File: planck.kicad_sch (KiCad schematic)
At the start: 53 parts, among them J1 USB_C_Receptacle_USB2.0, K1 KEYSW, K2 KEYSW, K3 KEYSW, K4 KEYSW, SW1 SW_PUSH, U1 ATmega32U4-M, Y1 Crystal_GND24_Small

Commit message: finishing it off
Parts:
- removed TP10: PB5, TestPoint:TestPoint_Pad_D1.0mm, symbol Connector:TestPoint
- removed TP11: PB6, TestPoint:TestPoint_Pad_D1.0mm, symbol Connector:TestPoint
- removed TP12: PB7, TestPoint:TestPoint_Pad_D1.0mm, symbol Connector:TestPoint
- removed TP13: PC6, TestPoint:TestPoint_Pad_D1.0mm, symbol Connector:TestPoint
- removed TP14: PC7, TestPoint:TestPoint_Pad_D1.0mm, symbol Connector:TestPoint
- removed TP15: PD0, TestPoint:TestPoint_Pad_D1.0mm, symbol Connector:TestPoint
- removed TP16: PD1, TestPoint:TestPoint_Pad_D1.0mm, symbol Connector:TestPoint
- removed TP17: PD2, TestPoint:TestPoint_Pad_D1.0mm, symbol Connector:TestPoint
- removed TP18: PD3, TestPoint:TestPoint_Pad_D1.0mm, symbol Connector:TestPoint
- removed TP19: PD4, TestPoint:TestPoint_Pad_D1.0mm, symbol Connector:TestPoint
- removed TP20: PD6, TestPoint:TestPoint_Pad_D1.0mm, symbol Connector:TestPoint
- removed TP21: PD7, TestPoint:TestPoint_Pad_D1.0mm, symbol Connector:TestPoint
- removed TP22: PE6, TestPoint:TestPoint_Pad_D1.0mm, symbol Connector:TestPoint
- removed TP23: PF6, TestPoint:TestPoint_Pad_D1.0mm, symbol Connector:TestPoint
- removed TP24: PF7, TestPoint:TestPoint_Pad_D1.0mm, symbol Connector:TestPoint
- removed TP4: PD5, TestPoint:TestPoint_Pad_D1.0mm, symbol Connector:TestPoint
- removed TP5: PB0, TestPoint:TestPoint_Pad_D1.0mm, symbol Connector:TestPoint
- removed TP6: PB1, TestPoint:TestPoint_Pad_D1.0mm, symbol Connector:TestPoint
- removed TP7: PB2, TestPoint:TestPoint_Pad_D1.0mm, symbol Connector:TestPoint
- removed TP8: PB3, TestPoint:TestPoint_Pad_D1.0mm, symbol Connector:TestPoint
- removed TP9: PB4, TestPoint:TestPoint_Pad_D1.0mm, symbol Connector:TestPoint
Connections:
- net PB0: no longer names the net of U1.8 (PB0)
- net PB1: no longer names the net of U1.9 (PB1)
- net PB2: no longer names the net of U1.10 (PB2)
- net PB3: no longer names the net of U1.11 (PB3)
- net PB4: no longer names the net of U1.28 (PB4)
- net PB5: no longer names the net of U1.29 (PB5)
- net PB6: no longer names the net of U1.30 (PB6)
- net PB7: no longer names the net of U1.12 (PB7)
- net PC6: no longer names the net of U1.31 (PC6)
- net PC7: no longer names the net of U1.32 (PC7)
- net PD0: no longer names the net of U1.18 (PD0)
- net PD1: no longer names the net of U1.19 (PD1)
- net PD2: no longer names the net of U1.20 (PD2)
- net PD3: no longer names the net of U1.21 (PD3)
- net PD4: no longer names the net of U1.25 (PD4)
- net PD5: no longer names the net of U1.22 (PD5)
- net PD6: no longer names the net of U1.26 (PD6)
- net PD7: no longer names the net of U1.27 (PD7)
- net PE6: no longer names the net of U1.1 (PE6)
- net PF6: no longer names the net of U1.37 (PF6)
- net PF7: no longer names the net of U1.36 (PF7)
- no-connect marks 0 -> 21

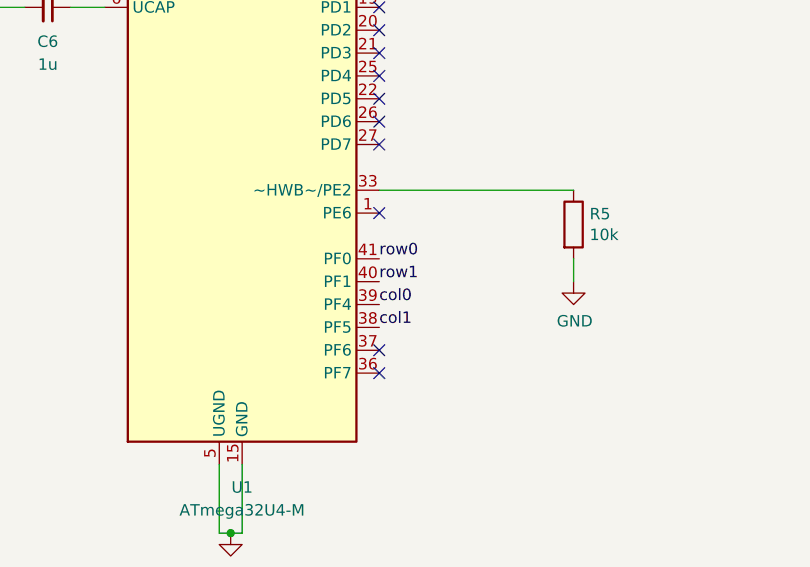
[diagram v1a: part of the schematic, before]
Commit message: switched pins for switches
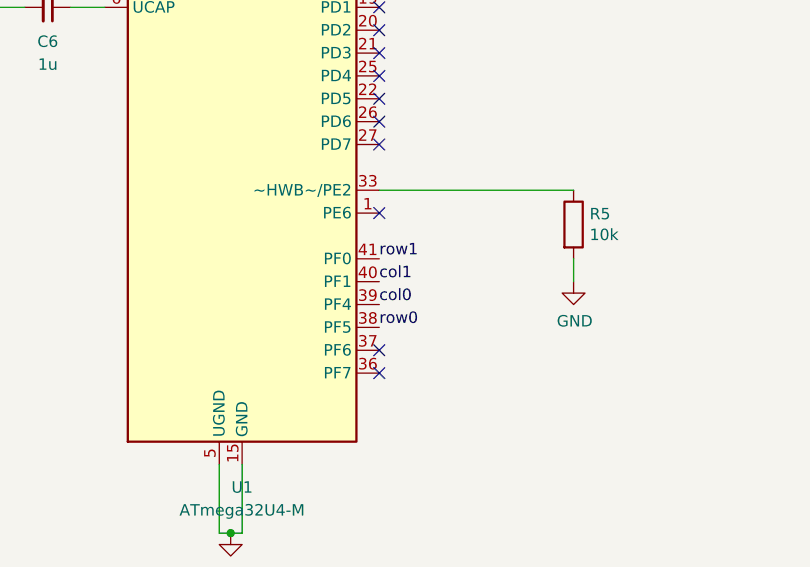
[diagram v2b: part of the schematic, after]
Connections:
- net col1: now also U1.40 (PF1); no longer U1.38 (PF5)
- net row0: now also U1.38 (PF5); no longer U1.41 (PF0)
- net row1: now also U1.41 (PF0); no longer U1.40 (PF1)
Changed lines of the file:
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@@
     (effects (font (size 1.27 1.27)) (justify right bottom))
   )
-  (label "row0" (at 165.1 118.11 0)
+  (label "row1" (at 165.1 118.11 0)
     (effects (font (size 1.27 1.27)) (justify left bottom))
   )
-  (label "row1" (at 165.1 120.65 0)
+  (label "col1" (at 165.1 120.65 0)
     (effects (font (size 1.27 1.27)) (justify left bottom))
   )
@@
     (effects (font (size 1.27 1.27)) (justify left bottom))
   )
-  (label "col1" (at 165.1 125.73 0)
+  (label "row0" (at 165.1 125.73 0)
     (effects (font (size 1.27 1.27)) (justify left bottom))
   )

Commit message: finished layout
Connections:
- net col0: now also U1.40 (PF1); no longer U1.39 (PF4)
- net col1: now also U1.38 (PF5); no longer U1.40 (PF1)
- net row0: now also U1.39 (PF4); no longer U1.38 (PF5)
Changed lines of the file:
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@@
     (effects (font (size 1.27 1.27)) (justify left bottom))
   )
-  (label "col1" (at 165.1 120.65 0)
+  (label "col0" (at 165.1 120.65 0)
     (effects (font (size 1.27 1.27)) (justify left bottom))
   )
-  (label "col0" (at 165.1 123.19 0)
+  (label "row0" (at 165.1 123.19 0)
     (effects (font (size 1.27 1.27)) (justify left bottom))
   )
-  (label "row0" (at 165.1 125.73 0)
+  (label "col1" (at 165.1 125.73 0)
     (effects (font (size 1.27 1.27)) (justify left bottom))
   )

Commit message: added digikey library
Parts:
- C1, C2, C3, C4, C5, C6, C7, C8, C9: footprint Capacitor_SMD:C_0603_1608Metric -> Capacitor_SMD:C_0402_1005Metric
- R1, R2, R3, R4, R5, R6: footprint Resistor_SMD:R_0603_1608Metric -> Resistor_SMD:R_0402_1005Metric
- SW1: footprint Button_Switch_SMD:SW_SPST_TL3342 -> Button_Switch_SMD:SW_SPST_CK_RS282G05A3
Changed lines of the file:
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@@
     (property "Reference" "R1" (id 0) (at 68.58 78.74 90))
     (property "Value" "5k1" (id 1) (at 68.58 81.28 90))
-    (property "Footprint" "Resistor_SMD:R_0603_1608Metric" (id 2) (at 68.58 83.312 90)
+    (property "Footprint" "Resistor_SMD:R_0402_1005Metric" (id 2) (at 68.58 83.312 90)
       (effects (font (size 1.27 1.27)) hide)
     )
@@
     (property "Reference" "R2" (id 0) (at 68.58 91.44 90))
     (property "Value" "5k1" (id 1) (at 68.58 93.98 90))
-    (property "Footprint" "Resistor_SMD:R_0603_1608Metric" (id 2) (at 68.58 85.852 90)
+    (property "Footprint" "Resistor_SMD:R_0402_1005Metric" (id 2) (at 68.58 85.852 90)
       (effects (font (size 1.27 1.27)) hide)
     )
@@
     (property "Reference" "R3" (id 0) (at 86.36 90.17 90))
     (property "Value" "22" (id 1) (at 86.36 92.71 90))
-    (property "Footprint" "Resistor_SMD:R_0603_1608Metric" (id 2) (at 86.36 93.472 90)
+    (property "Footprint" "Resistor_SMD:R_0402_1005Metric" (id 2) (at 86.36 93.472 90)
       (effects (font (size 1.27 1.27)) hide)
     )
@@
     (property "Reference" "R4" (id 0) (at 86.36 100.33 90))
     (property "Value" "22" (id 1) (at 86.36 102.87 90))
-    (property "Footprint" "Resistor_SMD:R_0603_1608Metric" (id 2) (at 86.36 96.012 90)
+    (property "Footprint" "Resistor_SMD:R_0402_1005Metric" (id 2) (at 86.36 96.012 90)
       (effects (font (size 1.27 1.27)) hide)
     )
@@
       (effects (font (size 1.27 1.27)) (justify left))
     )
-    (property "Footprint" "Resistor_SMD:R_0603_1608Metric" (id 2) (at 184.912 114.3 90)
+    (property "Footprint" "Resistor_SMD:R_0402_1005Metric" (id 2) (at 184.912 114.3 90)
       (effects (font (size 1.27 1.27)) hide)
     )
@@
       (effects (font (size 1.27 1.27)) (justify left))
     )
-    (property "Footprint" "Resistor_SMD:R_0603_1608Metric" (id 2) (at 253.492 36.83 90)
+    (property "Footprint" "Resistor_SMD:R_0402_1005Metric" (id 2) (at 253.492 36.83 90)
       (effects (font (size 1.27 1.27)) hide)
     )
@@
       (effects (font (size 1.27 1.27)) (justify left))
     )
-    (property "Footprint" "Capacitor_SMD:C_0603_1608Metric" (id 2) (at 34.29 35.56 0)
+    (property "Footprint" "Capacitor_SMD:C_0402_1005Metric" (id 2) (at 34.29 35.56 0)
       (effects (font (size 1.27 1.27)) hide)
     )
@@
       (effects (font (size 1.27 1.27)) (justify left))
     )
-    (property "Footprint" "Capacitor_SMD:C_0603_1608Metric" (id 2) (at 43.18 35.56 0)
+    (property "Footprint" "Capacitor_SMD:C_0402_1005Metric" (id 2) (at 43.18 35.56 0)
       (effects (font (size 1.27 1.27)) hide)
     )
@@
       (effects (font (size 1.27 1.27)) (justify left))
     )
-    (property "Footprint" "Capacitor_SMD:C_0603_1608Metric" (id 2) (at 52.07 35.56 0)
+    (property "Footprint" "Capacitor_SMD:C_0402_1005Metric" (id 2) (at 52.07 35.56 0)
       (effects (font (size 1.27 1.27)) hide)
     )
@@
       (effects (font (size 1.27 1.27)) (justify left))
     )
-    (property "Footprint" "Capacitor_SMD:C_0603_1608Metric" (id 2) (at 60.96 35.56 0)
+    (property "Footprint" "Capacitor_SMD:C_0402_1005Metric" (id 2) (at 60.96 35.56 0)
       (effects (font (size 1.27 1.27)) hide)
     )
@@
       (effects (font (size 1.27 1.27)) (justify left))
     )
-    (property "Footprint" "Capacitor_SMD:C_0603_1608Metric" (id 2) (at 69.85 35.56 0)
+    (property "Footprint" "Capacitor_SMD:C_0402_1005Metric" (id 2) (at 69.85 35.56 0)
       (effects (font (size 1.27 1.27)) hide)
     )
@@
     (property "Reference" "C6" (id 0) (at 128.27 93.98 90))
     (property "Value" "1u" (id 1) (at 128.27 96.52 90))
-    (property "Footprint" "Capacitor_SMD:C_0603_1608Metric" (id 2) (at 128.27 90.17 0)
+    (property "Footprint" "Capacitor_SMD:C_0402_1005Metric" (id 2) (at 128.27 90.17 0)
       (effects (font (size 1.27 1.27)) hide)
     )
@@
       (effects (font (size 1.27 1.27)) (justify left))
     )
-    (property "Footprint" "Capacitor_SMD:C_0603_1608Metric" (id 2) (at 233.68 132.08 0)
+    (property "Footprint" "Capacitor_SMD:C_0402_1005Metric" (id 2) (at 233.68 132.08 0)
       (effects (font (size 1.27 1.27)) hide)
     )
@@
       (effects (font (size 1.27 1.27)) (justify left))
     )
-    (property "Footprint" "Capacitor_SMD:C_0603_1608Metric" (id 2) (at 245.11 52.07 0)
+    (property "Footprint" "Capacitor_SMD:C_0402_1005Metric" (id 2) (at 245.11 52.07 0)
       (effects (font (size 1.27 1.27)) hide)
     )
@@
       (effects (font (size 1.27 1.27)) (justify left))
     )
-    (property "Footprint" "Capacitor_SMD:C_0603_1608Metric" (id 2) (at 252.73 132.08 0)
+    (property "Footprint" "Capacitor_SMD:C_0402_1005Metric" (id 2) (at 252.73 132.08 0)
       (effects (font (size 1.27 1.27)) hide)
     )
@@
       (effects (font (size 1.27 1.27)) (justify left))
     )
-    (property "Footprint" "Button_Switch_SMD:SW_SPST_TL3342" (id 2) (at 255.27 52.07 0)
+    (property "Footprint" "Button_Switch_SMD:SW_SPST_CK_RS282G05A3" (id 2) (at 255.27 52.07 0)
       (effects (font (size 1.524 1.524)) hide)
     )
@@
     )
     (path "/00000000-0000-0000-0000-000060c3a560"
-      (reference "C1") (unit 1) (value "0.1u") (footprint "Capacitor_SMD:C_0603_1608Metric")
+      (reference "C1") (unit 1) (value "0.1u") (footprint "Capacitor_SMD:C_0402_1005Metric")
     )
     (path "/00000000-0000-0000-0000-000060c3a91f"
-      (reference "C2") (unit 1) (value "0.1u") (footprint "Capacitor_SMD:C_0603_1608Metric")
+      (reference "C2") (unit 1) (value "0.1u") (footprint "Capacitor_SMD:C_0402_1005Metric")
     )
     (path "/00000000-0000-0000-0000-000060c3af02"
-      (reference "C3") (unit 1) (value "0.1u") (footprint "Capacitor_SMD:C_0603_1608Metric")
+      (reference "C3") (unit 1) (value "0.1u") (footprint "Capacitor_SMD:C_0402_1005Metric")
     )
     (path "/00000000-0000-0000-0000-000060c3b232"
-      (reference "C4") (unit 1) (value "0.1u") (footprint "Capacitor_SMD:C_0603_1608Metric")
+      (reference "C4") (unit 1) (value "0.1u") (footprint "Capacitor_SMD:C_0402_1005Metric")
     )
     (path "/00000000-0000-0000-0000-000060c3b567"
-      (reference "C5") (unit 1) (value "4.7u") (footprint "Capacitor_SMD:C_0603_1608Metric")
+      (reference "C5") (unit 1) (value "4.7u") (footprint "Capacitor_SMD:C_0402_1005Metric")
     )
     (path "/00000000-0000-0000-0000-000060c6c4be"
-      (reference "C6") (unit 1) (value "1u") (footprint "Capacitor_SMD:C_0603_1608Metric")
+      (reference "C6") (unit 1) (value "1u") (footprint "Capacitor_SMD:C_0402_1005Metric")
     )
     (path "/00000000-0000-0000-0000-000060c2af38"
-      (reference "C7") (unit 1) (value "18p") (footprint "Capacitor_SMD:C_0603_1608Metric")
+      (reference "C7") (unit 1) (value "18p") (footprint "Capacitor_SMD:C_0402_1005Metric")
     )
     (path "/49a617b2-1c0c-4f9e-bd54-e1ccb8763dff"
-      (reference "C8") (unit 1) (value "0.1u") (footprint "Capacitor_SMD:C_0603_1608Metric")
+      (reference "C8") (unit 1) (value "0.1u") (footprint "Capacitor_SMD:C_0402_1005Metric")
     )
     (path "/00000000-0000-0000-0000-000060c2b474"
-      (reference "C9") (unit 1) (value "18p") (footprint "Capacitor_SMD:C_0603_1608Metric")
+      (reference "C9") (unit 1) (value "18p") (footprint "Capacitor_SMD:C_0402_1005Metric")
     )
     (path "/00000000-0000-0000-0000-000060cc759c"
@@
     )
     (path "/74efaa67-602b-4da7-8d93-ebd772d4838b"
-      (reference "R1") (unit 1) (value "5k1") (footprint "Resistor_SMD:R_0603_1608Metric")
+      (reference "R1") (unit 1) (value "5k1") (footprint "Resistor_SMD:R_0402_1005Metric")
     )
     (path "/d0c18c6c-c93d-4879-acfd-ddbccb5b307b"
-      (reference "R2") (unit 1) (value "5k1") (footprint "Resistor_SMD:R_0603_1608Metric")
+      (reference "R2") (unit 1) (value "5k1") (footprint "Resistor_SMD:R_0402_1005Metric")
     )
     (path "/00000000-0000-0000-0000-000060c72e0d"
-      (reference "R3") (unit 1) (value "22") (footprint "Resistor_SMD:R_0603_1608Metric")
+      (reference "R3") (unit 1) (value "22") (footprint "Resistor_SMD:R_0402_1005Metric")
     )
     (path "/00000000-0000-0000-0000-000060c7372f"
-      (reference "R4") (unit 1) (value "22") (footprint "Resistor_SMD:R_0603_1608Metric")
+      (reference "R4") (unit 1) (value "22") (footprint "Resistor_SMD:R_0402_1005Metric")
     )
     (path "/00000000-0000-0000-0000-000060c52c48"
-      (reference "R5") (unit 1) (value "10k") (footprint "Resistor_SMD:R_0603_1608Metric")
+      (reference "R5") (unit 1) (value "10k") (footprint "Resistor_SMD:R_0402_1005Metric")
     )
     (path "/00000000-0000-0000-0000-000060c4b284"
-      (reference "R6") (unit 1) (value "10k") (footprint "Resistor_SMD:R_0603_1608Metric")
+      (reference "R6") (unit 1) (value "10k") (footprint "Resistor_SMD:R_0402_1005Metric")
     )
     (path "/00000000-0000-0000-0000-000060c3ec5e"
-      (reference "SW1") (unit 1) (value "SW_PUSH") (footprint "Button_Switch_SMD:SW_SPST_TL3342")
+      (reference "SW1") (unit 1) (value "SW_PUSH") (footprint "Button_Switch_SMD:SW_SPST_CK_RS282G05A3")
     )
     (path "/c932b45d-2ece-414c-9c1a-1ac052e35eb0"

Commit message: added new usb c
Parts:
- J1: footprint Connector_USB:USB_C_Receptacle_Amphenol_12401548E4-2A -> Connector_USB:USB_C_Receptacle_Amphenol_12401610E4-2A
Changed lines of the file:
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@@
     (property "Reference" "J1" (id 0) (at 45.847 73.66 0))
     (property "Value" "USB_C_Receptacle_USB2.0" (id 1) (at 45.847 76.2 0))
-    (property "Footprint" "Connector_USB:USB_C_Receptacle_Amphenol_12401548E4-2A" (id 2) (at 46.99 95.25 0)
+    (property "Footprint" "Connector_USB:USB_C_Receptacle_Amphenol_12401610E4-2A" (id 2) (at 46.99 95.25 0)
       (effects (font (size 1.27 1.27)) hide)
     )
@@
     )
     (path "/a3d25767-1c49-4406-bdf0-59c6d7959960"
-      (reference "J1") (unit 1) (value "USB_C_Receptacle_USB2.0") (footprint "Connector_USB:USB_C_Receptacle_Amphenol_12401548E4-2A")
+      (reference "J1") (unit 1) (value "USB_C_Receptacle_USB2.0") (footprint "Connector_USB:USB_C_Receptacle_Amphenol_12401610E4-2A")
     )
     (path "/00000000-0000-0000-0000-000060cc5874"
